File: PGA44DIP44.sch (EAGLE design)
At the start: 9 parts, among them CN1 JTAG, IC1 LM2937ET-3.3/NOPB

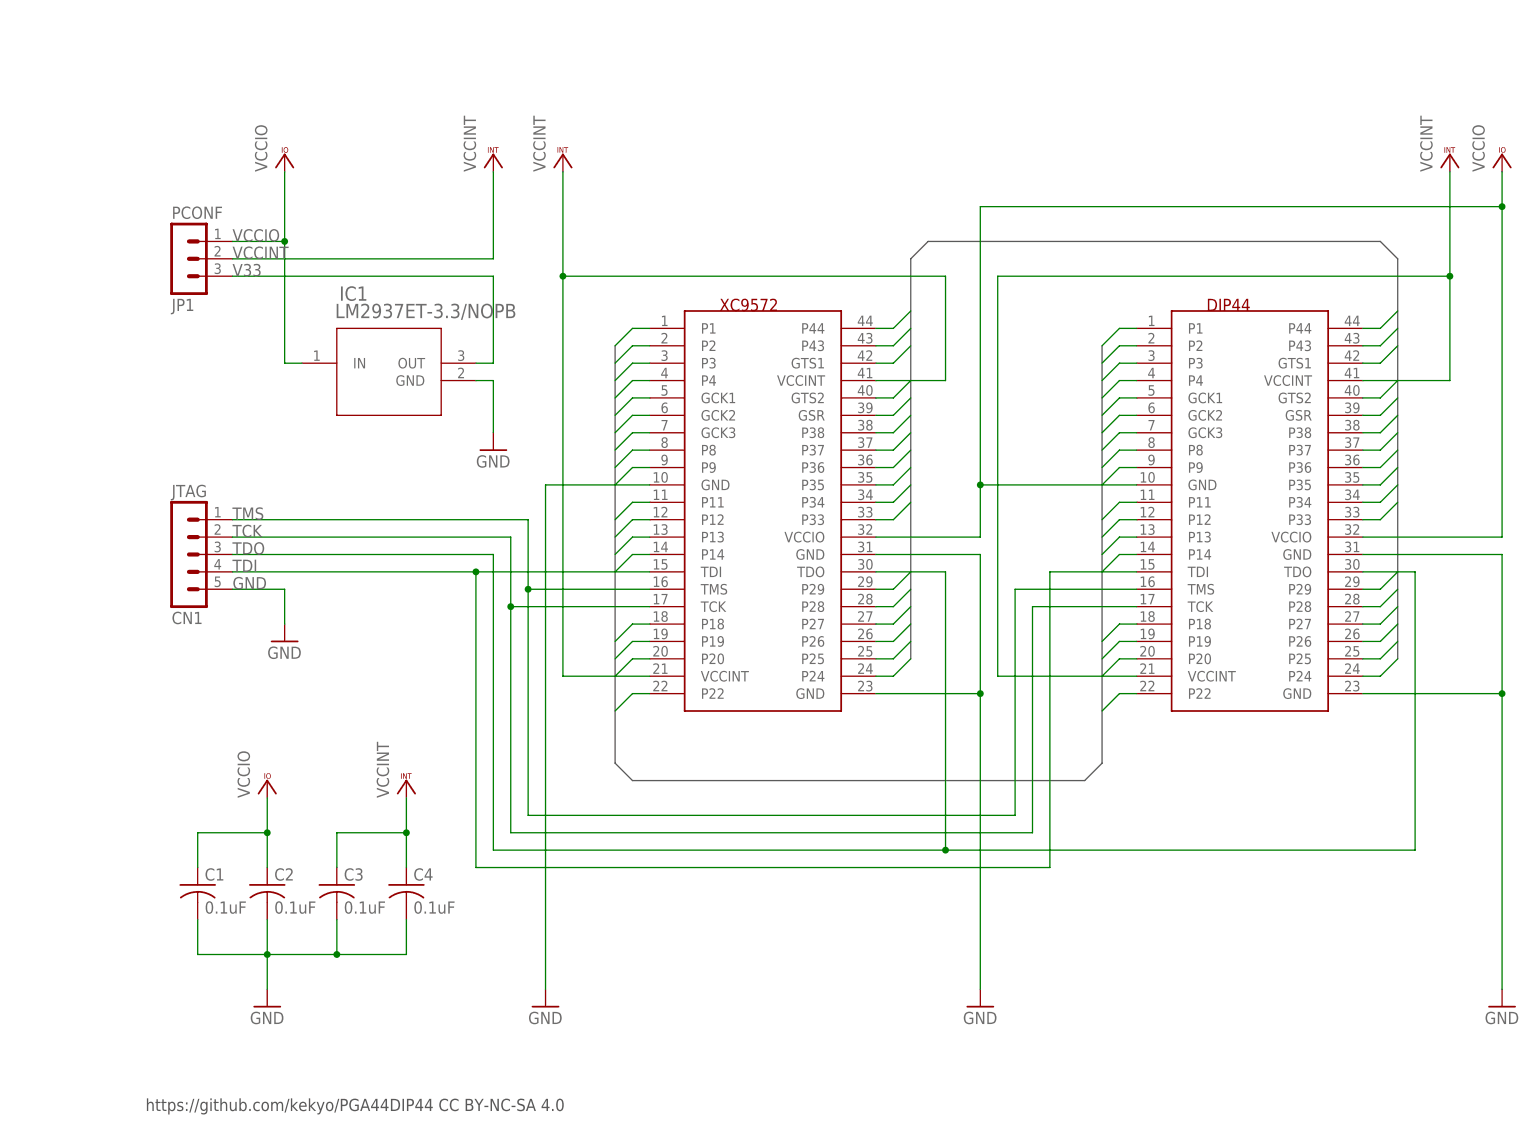
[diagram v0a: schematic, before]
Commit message: * Improve ground patterns. * Improve signal lines.
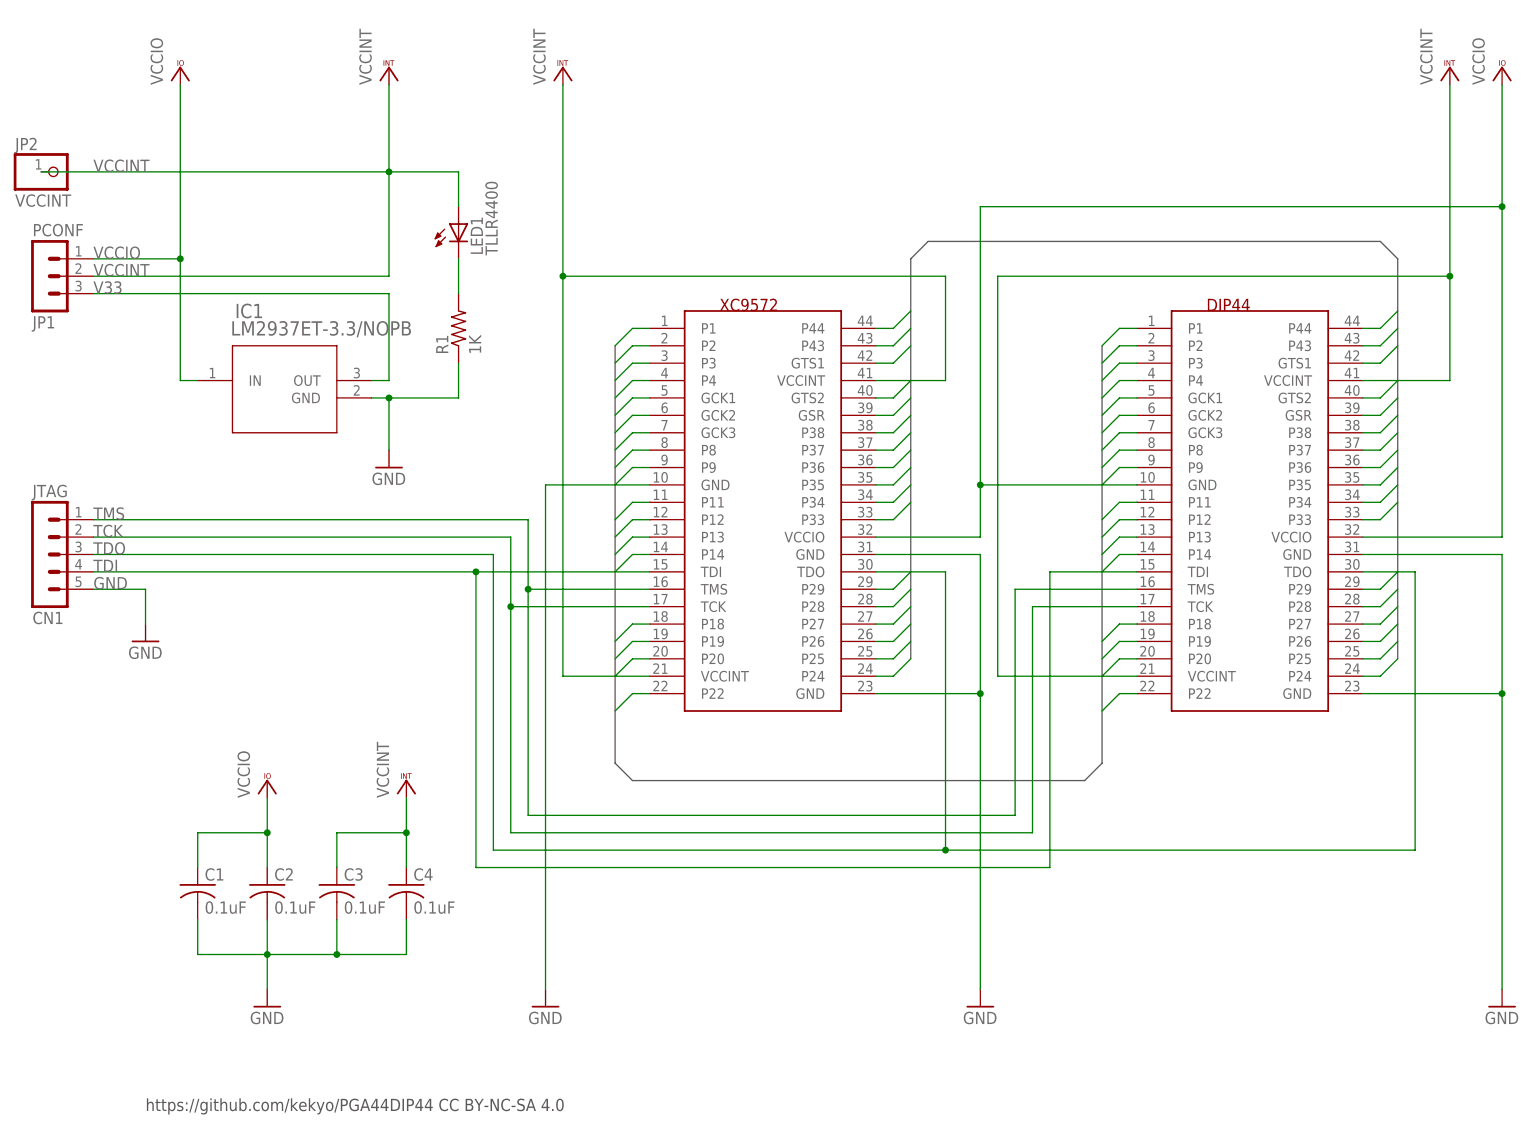
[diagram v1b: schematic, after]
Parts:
- added JP2: VCCINT, PGA44DIP44:PINHD-1X1
- added LED1: TLLR4400, PGA44DIP44:TLLR4400
- added R1: 1K, PGA44DIP44:R-US_0207/2V
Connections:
- new net N$1: LED1.C, R1.2
- net GND: now also R1.1
- net VCCINT: now also JP2.1, LED1.A
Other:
- moved on the sheet: CN1, IC1, JP1
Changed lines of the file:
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@@
 <?xml version="1.0" encoding="utf-8"?>
 <!DOCTYPE eagle SYSTEM "eagle.dtd">
-<eagle version="8.1.0">
+<eagle version="8.1.1">
 <drawing>
 <settings>
@@
 <part name="JP1" library="PGA44DIP44" deviceset="MA03-1" device="" value="PCONF"/>
 <part name="CN1" library="PGA44DIP44" deviceset="MA05-1" device="" value="JTAG"/>
+<part name="JP2" library="PGA44DIP44" deviceset="PINHD-1X1" device="" value="VCCINT"/>
+<part name="R1" library="PGA44DIP44" deviceset="R-US_" device="0207/2V" value="1K"/>
+<part name="LED1" library="PGA44DIP44" deviceset="TLLR4400" device=""/>
 </parts>
 <sheets>
@@
 </plain>
 <instances>
-<instance part="VCC1" gate="G$1" x="68.58" y="144.78"/>
-<instance part="VCC2" gate="G$1" x="198.12" y="144.78"/>
-<instance part="VCC3" gate="G$1" x="205.74" y="144.78"/>
+<instance part="VCC1" gate="G$1" x="68.58" y="157.48"/>
+<instance part="VCC2" gate="G$1" x="198.12" y="157.48"/>
+<instance part="VCC3" gate="G$1" x="205.74" y="157.48"/>
 <instance part="GND1" gate="1" x="205.74" y="20.32"/>
 <instance part="GND3" gate="1" x="66.04" y="20.32"/>
-<instance part="IC1" gate="A" x="43.18" y="114.3"/>
-<instance part="VCC4" gate="G$1" x="27.94" y="144.78"/>
-<instance part="VCC5" gate="G$1" x="58.42" y="144.78"/>
-<instance part="GND4" gate="1" x="58.42" y="101.6"/>
+<instance part="IC1" gate="A" x="27.94" y="111.76"/>
+<instance part="VCC4" gate="G$1" x="12.7" y="157.48"/>
+<instance part="VCC5" gate="G$1" x="43.18" y="157.48"/>
+<instance part="GND4" gate="1" x="43.18" y="99.06"/>
 <instance part="C1" gate="G$1" x="15.24" y="38.1"/>
 <instance part="C2" gate="G$1" x="25.4" y="38.1"/>
@@
 <instance part="VCC6" gate="G$1" x="25.4" y="53.34"/>
 <instance part="VCC7" gate="G$1" x="45.72" y="53.34"/>
-<instance part="GND6" gate="1" x="27.94" y="73.66"/>
+<instance part="GND6" gate="1" x="7.62" y="73.66"/>
 <instance part="XC9572" gate="XC9572" x="93.98" y="93.98"/>
 <instance part="DIP44" gate="G$1" x="165.1" y="93.98"/>
 <instance part="GND7" gate="1" x="129.54" y="20.32"/>
-<instance part="JP1" gate="G$1" x="12.7" y="129.54" rot="MR180"/>
-<instance part="CN1" gate="G$1" x="12.7" y="86.36" rot="MR180"/>
+<instance part="JP1" gate="G$1" x="-7.62" y="127" rot="MR180"/>
+<instance part="CN1" gate="G$1" x="-7.62" y="86.36" rot="MR180"/>
+<instance part="JP2" gate="G$1" x="-5.08" y="142.24"/>
+<instance part="R1" gate="G$1" x="53.34" y="119.38" rot="R90"/>
+<instance part="LED1" gate="G$1" x="53.34" y="134.62"/>
 </instances>
 <busses>
@@
 <net name="TDI" class="0">
 <segment>
-<wire x1="20.32" y1="83.82" x2="55.88" y2="83.82" width="0.1524" layer="91"/>
-<label x="20.32" y="83.82" size="1.778" layer="95"/>
+<wire x1="0" y1="83.82" x2="55.88" y2="83.82" width="0.1524" layer="91"/>
+<label x="0" y="83.82" size="1.778" layer="95"/>
 <wire x1="55.88" y1="83.82" x2="55.88" y2="40.64" width="0.1524" layer="91"/>
 <wire x1="55.88" y1="40.64" x2="139.7" y2="40.64" width="0.1524" layer="91"/>
@@
 <wire x1="124.46" y1="43.18" x2="58.42" y2="43.18" width="0.1524" layer="91"/>
 <wire x1="58.42" y1="43.18" x2="58.42" y2="86.36" width="0.1524" layer="91"/>
-<wire x1="58.42" y1="86.36" x2="20.32" y2="86.36" width="0.1524" layer="91"/>
-<label x="20.32" y="86.36" size="1.778" layer="95"/>
+<wire x1="58.42" y1="86.36" x2="0" y2="86.36" width="0.1524" layer="91"/>
+<label x="0" y="86.36" size="1.778" layer="95"/>
 <wire x1="124.46" y1="83.82" x2="124.46" y2="43.18" width="0.1524" layer="91"/>
 <pinref part="DIP44" gate="G$1" pin="TDO"/>
@@
 <segment>
 <pinref part="VCC4" gate="G$1" pin="VCCIO"/>
-<wire x1="27.94" y1="142.24" x2="27.94" y2="132.08" width="0.1524" layer="91"/>
+<wire x1="12.7" y1="154.94" x2="12.7" y2="129.54" width="0.1524" layer="91"/>
 <pinref part="IC1" gate="A" pin="IN"/>
-<wire x1="27.94" y1="132.08" x2="27.94" y2="114.3" width="0.1524" layer="91"/>
-<wire x1="27.94" y1="114.3" x2="30.48" y2="114.3" width="0.1524" layer="91"/>
-<wire x1="20.32" y1="132.08" x2="27.94" y2="132.08" width="0.1524" layer="91"/>
-<junction x="27.94" y="132.08"/>
+<wire x1="12.7" y1="129.54" x2="12.7" y2="111.76" width="0.1524" layer="91"/>
+<wire x1="12.7" y1="111.76" x2="15.24" y2="111.76" width="0.1524" layer="91"/>
+<wire x1="0" y1="129.54" x2="12.7" y2="129.54" width="0.1524" layer="91"/>
+<junction x="12.7" y="129.54"/>
 <pinref part="JP1" gate="G$1" pin="1"/>
-<label x="20.32" y="132.08" size="1.778" layer="95"/>
+<label x="0" y="129.54" size="1.778" layer="95"/>
 </segment>
 <segment>
@@
 <pinref part="DIP44" gate="G$1" pin="VCCIO"/>
 <pinref part="XC9572" gate="XC9572" pin="VCCIO"/>
-<wire x1="205.74" y1="137.16" x2="205.74" y2="142.24" width="0.1524" layer="91"/>
+<wire x1="205.74" y1="137.16" x2="205.74" y2="154.94" width="0.1524" layer="91"/>
 <wire x1="114.3" y1="88.9" x2="129.54" y2="88.9" width="0.1524" layer="91"/>
 <wire x1="129.54" y1="88.9" x2="129.54" y2="96.52" width="0.1524" layer="91"/>
@@
 <segment>
 <pinref part="GND4" gate="1" pin="GND"/>
-<wire x1="58.42" y1="104.14" x2="58.42" y2="111.76" width="0.1524" layer="91"/>
+<wire x1="43.18" y1="101.6" x2="43.18" y2="109.22" width="0.1524" layer="91"/>
 <pinref part="IC1" gate="A" pin="GND"/>
-<wire x1="58.42" y1="111.76" x2="55.88" y2="111.76" width="0.1524" layer="91"/>
+<wire x1="43.18" y1="109.22" x2="40.64" y2="109.22" width="0.1524" layer="91"/>
+<wire x1="43.18" y1="109.22" x2="53.34" y2="109.22" width="0.1524" layer="91"/>
+<junction x="43.18" y="109.22"/>
+<wire x1="53.34" y1="109.22" x2="53.34" y2="114.3" width="0.1524" layer="91"/>
+<pinref part="R1" gate="G$1" pin="1"/>
 </segment>
 <segment>
@@
 </segment>
 <segment>
-<wire x1="20.32" y1="81.28" x2="27.94" y2="81.28" width="0.1524" layer="91"/>
+<wire x1="0" y1="81.28" x2="7.62" y2="81.28" width="0.1524" layer="91"/>
 <pinref part="GND6" gate="1" pin="GND"/>
-<wire x1="27.94" y1="81.28" x2="27.94" y2="76.2" width="0.1524" layer="91"/>
-<label x="20.32" y="81.28" size="1.778" layer="95"/>
+<wire x1="7.62" y1="81.28" x2="7.62" y2="76.2" width="0.1524" layer="91"/>
+<label x="0" y="81.28" size="1.778" layer="95"/>
 <pinref part="CN1" gate="G$1" pin="5"/>
 </segment>
@@
 <segment>
 <pinref part="IC1" gate="A" pin="OUT"/>
-<wire x1="58.42" y1="114.3" x2="55.88" y2="114.3" width="0.1524" layer="91"/>
-<wire x1="58.42" y1="114.3" x2="58.42" y2="127" width="0.1524" layer="91"/>
-<wire x1="58.42" y1="127" x2="20.32" y2="127" width="0.1524" layer="91"/>
+<wire x1="43.18" y1="111.76" x2="40.64" y2="111.76" width="0.1524" layer="91"/>
+<wire x1="43.18" y1="111.76" x2="43.18" y2="124.46" width="0.1524" layer="91"/>
+<wire x1="43.18" y1="124.46" x2="0" y2="124.46" width="0.1524" layer="91"/>
 <pinref part="JP1" gate="G$1" pin="3"/>
-<label x="20.32" y="127" size="1.778" layer="95"/>
+<label x="0" y="124.46" size="1.778" layer="95"/>
 </segment>
 </net>
@@
 <segment>
 <pinref part="VCC5" gate="G$1" pin="VCCINT"/>
-<wire x1="58.42" y1="142.24" x2="58.42" y2="129.54" width="0.1524" layer="91"/>
-<wire x1="20.32" y1="129.54" x2="58.42" y2="129.54" width="0.1524" layer="91"/>
+<wire x1="43.18" y1="154.94" x2="43.18" y2="142.24" width="0.1524" layer="91"/>
+<wire x1="43.18" y1="142.24" x2="43.18" y2="127" width="0.1524" layer="91"/>
+<wire x1="0" y1="127" x2="43.18" y2="127" width="0.1524" layer="91"/>
 <pinref part="JP1" gate="G$1" pin="2"/>
-<label x="20.32" y="129.54" size="1.778" layer="95"/>
+<label x="0" y="127" size="1.778" layer="95"/>
+<junction x="43.18" y="142.24"/>
+<label x="0" y="142.24" size="1.778" layer="95"/>
+<wire x1="43.18" y1="142.24" x2="53.34" y2="142.24" width="0.1524" layer="91"/>
+<wire x1="53.34" y1="142.24" x2="53.34" y2="137.16" width="0.1524" layer="91"/>
+<pinref part="JP2" gate="G$1" pin="1"/>
+<wire x1="-7.62" y1="142.24" x2="43.18" y2="142.24" width="0.1524" layer="91"/>
+<pinref part="LED1" gate="G$1" pin="A"/>
 </segment>
 <segment>
@@
 <pinref part="VCC1" gate="G$1" pin="VCCINT"/>
 <pinref part="XC9572" gate="XC9572" pin="VCCINT@1"/>
-<wire x1="68.58" y1="127" x2="68.58" y2="142.24" width="0.1524" layer="91"/>
+<wire x1="68.58" y1="127" x2="68.58" y2="154.94" width="0.1524" layer="91"/>
 <wire x1="68.58" y1="68.58" x2="81.28" y2="68.58" width="0.1524" layer="91"/>
 <pinref part="XC9572" gate="XC9572" pin="VCCINT@2"/>
@@
 <pinref part="DIP44" gate="G$1" pin="VCCINT@2"/>
 <wire x1="198.12" y1="111.76" x2="198.12" y2="127" width="0.1524" layer="91"/>
-<wire x1="198.12" y1="127" x2="198.12" y2="142.24" width="0.1524" layer="91"/>
+<wire x1="198.12" y1="127" x2="198.12" y2="154.94" width="0.1524" layer="91"/>
 <wire x1="185.42" y1="111.76" x2="198.12" y2="111.76" width="0.1524" layer="91"/>
 <pinref part="DIP44" gate="G$1" pin="VCCINT@1"/>
@@
 <wire x1="81.28" y1="81.28" x2="63.5" y2="81.28" width="0.1524" layer="91"/>
 <wire x1="63.5" y1="81.28" x2="63.5" y2="91.44" width="0.1524" layer="91"/>
-<wire x1="63.5" y1="91.44" x2="20.32" y2="91.44" width="0.1524" layer="91"/>
-<label x="20.32" y="91.44" size="1.778" layer="95"/>
+<wire x1="63.5" y1="91.44" x2="0" y2="91.44" width="0.1524" layer="91"/>
+<label x="0" y="91.44" size="1.778" layer="95"/>
 <wire x1="63.5" y1="81.28" x2="63.5" y2="48.26" width="0.1524" layer="91"/>
 <junction x="63.5" y="81.28"/>
@@
 <wire x1="81.28" y1="78.74" x2="60.96" y2="78.74" width="0.1524" layer="91"/>
 <wire x1="60.96" y1="78.74" x2="60.96" y2="88.9" width="0.1524" layer="91"/>
-<wire x1="60.96" y1="88.9" x2="20.32" y2="88.9" width="0.1524" layer="91"/>
-<label x="20.32" y="88.9" size="1.778" layer="95"/>
+<wire x1="60.96" y1="88.9" x2="0" y2="88.9" width="0.1524" layer="91"/>
+<label x="0" y="88.9" size="1.778" layer="95"/>
 <wire x1="60.96" y1="78.74" x2="60.96" y2="45.72" width="0.1524" layer="91"/>
 <junction x="60.96" y="78.74"/>
@@
 </segment>
 </net>
+<net name="N$1" class="0">
+<segment>
+<pinref part="LED1" gate="G$1" pin="C"/>
+<pinref part="R1" gate="G$1" pin="2"/>
+<wire x1="53.34" y1="129.54" x2="53.34" y2="124.46" width="0.1524" layer="91"/>
+</segment>
+</net>
